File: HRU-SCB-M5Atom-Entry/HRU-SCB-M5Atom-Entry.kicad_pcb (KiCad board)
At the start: 2 copper layers, 25.4 x 50.8 mm, 11 parts, among them J1 GROVE-CONNECTOR-DIP_4P-2.0_

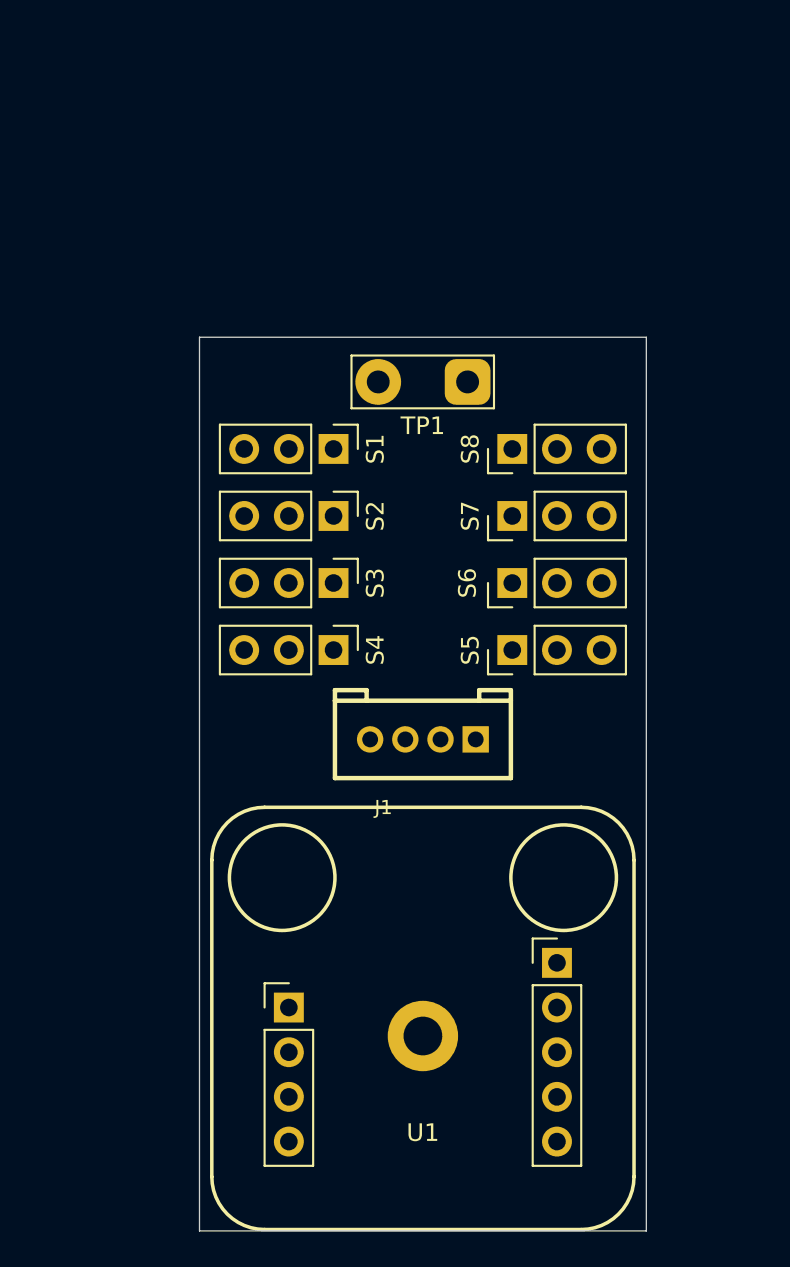
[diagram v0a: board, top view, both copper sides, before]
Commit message: Update: M5Atom entry board with Grove port
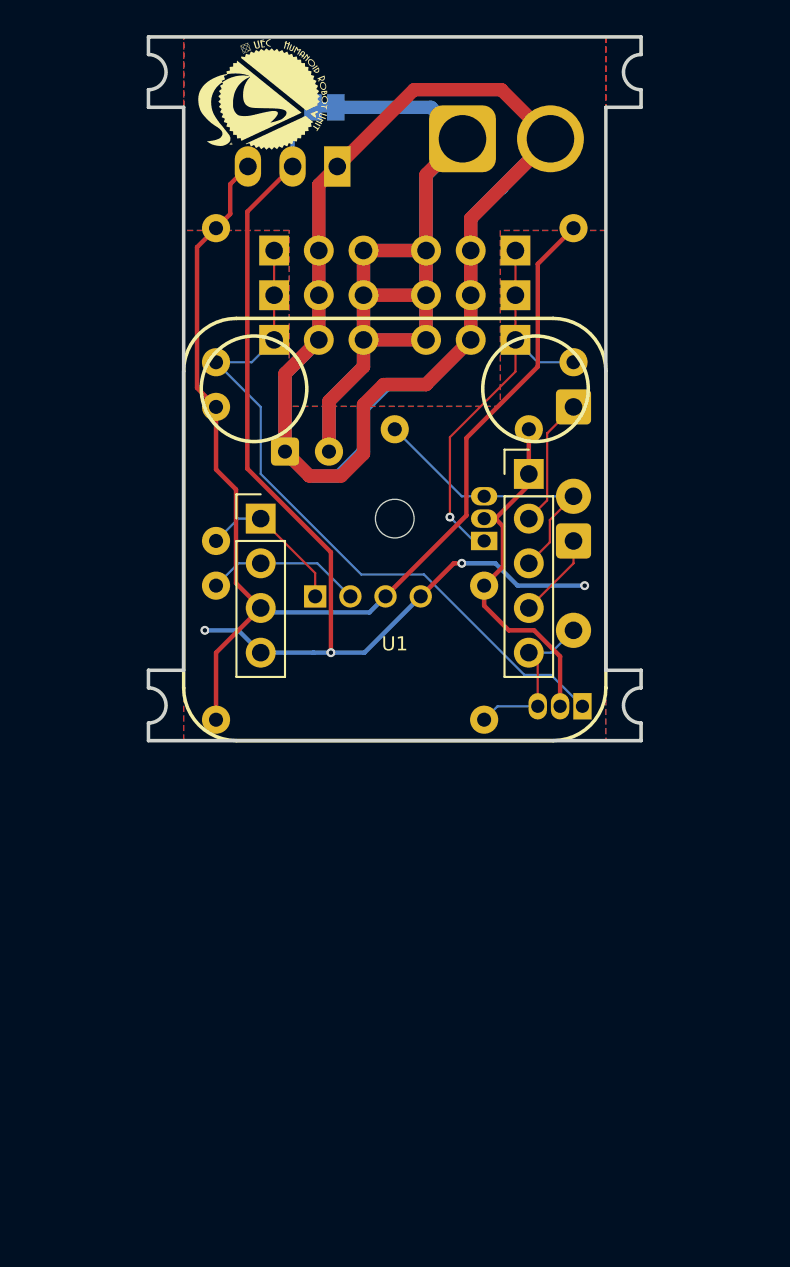
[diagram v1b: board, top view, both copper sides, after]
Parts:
- removed S7, S8: Conn_01x03_Pin, Connector_PinHeader_2.54mm:PinHeader_1x03_P2.54mm_Vertical
- removed TP1: TestPoint_2Pole, TestPoint:TestPoint_2Pads_Pitch5.08mm_Drill1.3mm
- added C1: 220uF, Capacitor_THT:CP_Radial_D6.3mm_P2.50mm, B.Cu at (93.8, 52.2)
- added D1: 11EQS03L, Diode_THT:D_T-1_P5.08mm_Horizontal, B.Cu at (110.2, 49.7)
- added D2: 11EQS03L, Diode_THT:D_T-1_P5.08mm_Horizontal, B.Cu at (110.2, 57.3)
- added J2: GROVE-CONNECTOR-DIP-90D_4P-2.0_, OPL_Connector:GROVE-HW4-2.0-90D, B.Cu at (98.5, 63.6)
- added JP1: SolderJumper_2_Bridged, Jumper:SolderJumper-2_P1.3mm_Bridged_Pad1.0x1.5mm, B.Cu at (96.0, 32.6)
- added Q1: BS170, Package_TO_SOT_THT:TO-92_Inline, B.Cu at (105.1, 57.3)
- added Q2: BS170, Package_TO_SOT_THT:TO-92_Inline, B.Cu at (110.7, 66.7)
- added R1: 2.2k, Resistor_THT:R_Axial_DIN0207_L6.3mm_D2.5mm_P7.62mm_Horizontal, B.Cu at (107.6, 51.0)
- added R2: 2.2k, Resistor_THT:R_Axial_DIN0207_L6.3mm_D2.5mm_P7.62mm_Horizontal, B.Cu at (105.1, 59.8)
- added R3: 2.2k, Resistor_THT:R_Axial_DIN0207_L6.3mm_D2.5mm_P7.62mm_Horizontal, B.Cu at (110.2, 39.5)
- added R4: 2.2k, Resistor_THT:R_Axial_DIN0207_L6.3mm_D2.5mm_P7.62mm_Horizontal, B.Cu at (89.8, 39.5)
- added R5: 2.2k, Resistor_THT:R_Axial_DIN0207_L6.3mm_D2.5mm_P7.62mm_Horizontal, B.Cu at (89.8, 49.7)
- added R6: 2.2k, Resistor_THT:R_Axial_DIN0207_L6.3mm_D2.5mm_P7.62mm_Horizontal, B.Cu at (89.8, 67.5)
- added U2: R-785.0-0.5, Converter_DCDC:Converter_DCDC_RECOM_R-78E-0.5_THT, B.Cu at (96.7, 36.0)
- J1: value GROVE-CONNECTOR-DIP_4P-2.0_ -> Conn_01x02_Pin; footprint OPL_Connector:GROVE-HW4-2.0 -> Connector_AMASS:AMASS_XT30U-M_1x02_P5.0mm_Vertical; moved to B.Cu
- S1, S2, S3, S4, S5, S6: moved to B.Cu
- U1: value ~ -> M5Atom
- moved J1 34.2 mm to (103.8, 34.4), turned to 0 degrees
- moved U1 27.8 mm to (100.0, 63.6)
- moved S5 24.3 mm to (93.1, 43.3), turned to -90 degrees
- moved S6 23.2 mm to (93.1, 40.8), turned to -90 degrees
- moved S4 18.0 mm to (93.1, 45.9)
- moved S3 17.3 mm to (106.9, 45.9), turned to 90 degrees
- moved S2 16.3 mm to (106.9, 43.3), turned to 90 degrees
- moved S1 15.3 mm to (106.9, 40.8), turned to 90 degrees
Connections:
- J1 pad 1: unconnected-(J1-Pad1) -> GNDPWR
- J1 pad 2: unconnected-(J1-Pad2) -> VCC
- S1 pad 1: unconnected-(S1-Pin_1-Pad1) -> /SERVO.0
- S2 pad 1: unconnected-(S2-Pin_1-Pad1) -> /SERVO.0
- S3 pad 1: unconnected-(S3-Pin_1-Pad1) -> /SERVO.0
- S4 pad 1: /SERVO.0 -> /SERVO.1
- S5 pad 1: /SERVO.0 -> /SERVO.1
- S6 pad 1: /SERVO.0 -> /SERVO.1
- U1 pad 1: unconnected-(U1-SCL-Pad1) -> +3V3
- U1 pad 2: unconnected-(U1-SDA-Pad2) -> /Serial.0.TX
- U1 pad 3: unconnected-(U1-5V-Pad3) -> /Serial.0.RX
- U1 pad 4: GND -> /Serial.1.TX
- U1 pad 6: /Serial.1.TX -> GND
- U1 pad 7: /Serial.0.RX -> +5V
- U1 pad 8: /Serial.0.TX -> Net-(U1-SDA)
- U1 pad 9: unconnected-(U1-3V3-Pad9) -> Net-(U1-SCL)
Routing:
- net VCC: track 0.00 -> 108.4 mm
- net GNDPWR: track 0.00 -> 78.9 mm
- net +5V: track 0.00 -> 68.1 mm
- net GND: track 0.00 -> 59.3 mm, vias 0 -> 4
- net /SERVO.1: track 0.00 -> 40.1 mm
- net /SERVO.0: track 0.00 -> 23.0 mm, vias 0 -> 1
- net +3V3: track 0.00 -> 21.1 mm
- net /Serial.0.RX: track 0.00 -> 16.6 mm
- net /Serial.1.RX: track 0.00 -> 9.69 mm
- net Net-(U1-SDA): track 0.00 -> 8.94 mm
- net Net-(U1-SCL): track 0.00 -> 8.77 mm
- net /Serial.0.TX: track 0.00 -> 7.40 mm
- net /Serial.1.TX: track 0.00 -> 4.86 mm
- added copper zone on B.Cu, net GND
- added copper zone on F.Cu, net GND
- added copper zone on B.Cu, net GNDPWR
- added copper zone on F.Cu, net VCC
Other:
- board size 25.4 x 50.8 mm -> 28 x 40 mm
- board text added: "CH0"
- board text added: "CH1"
- board text added: "G"
- board text added: "V"

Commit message: Update: parts layout and smaller board
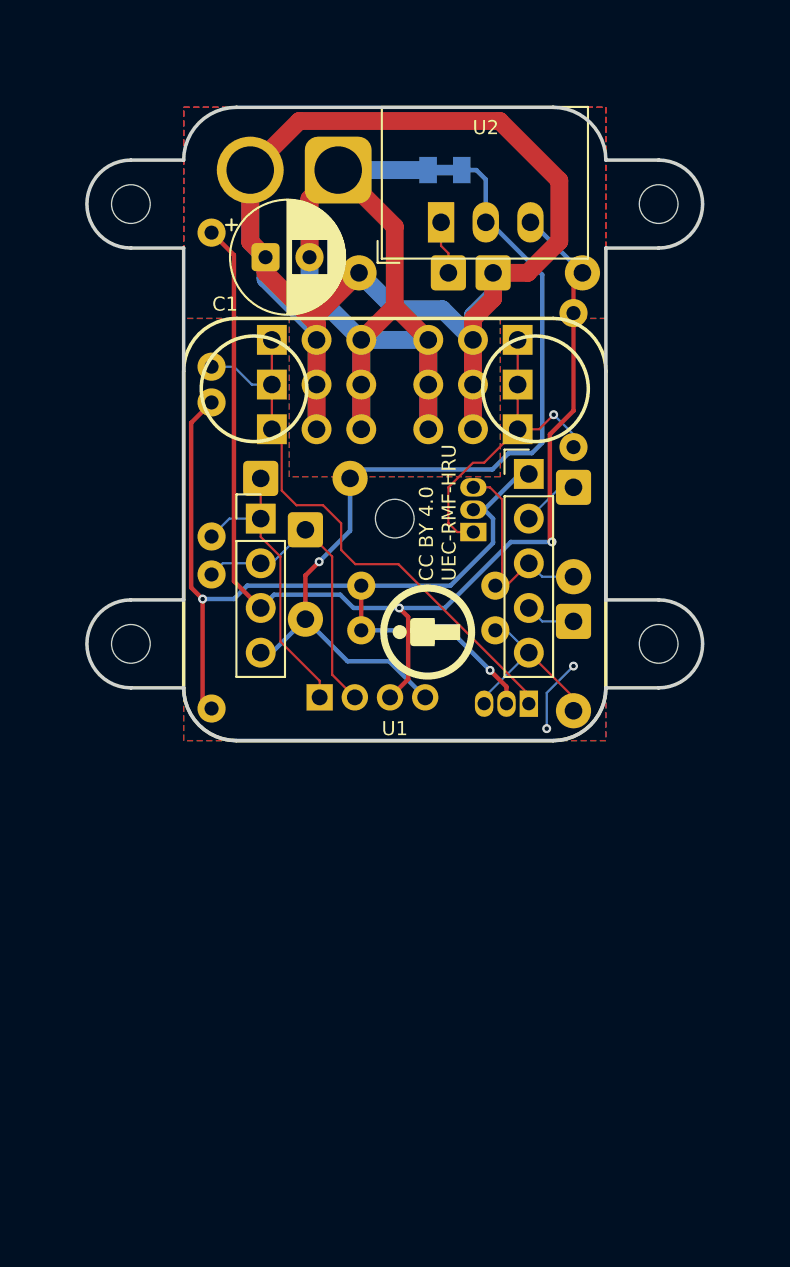
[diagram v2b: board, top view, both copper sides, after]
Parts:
- added D3: BZX55C3V3, Diode_THT:D_T-1_P5.08mm_Horizontal, B.Cu at (92.4, 53.7)
- added D4: BZX55C3V3, Diode_THT:D_T-1_P5.08mm_Horizontal, B.Cu at (94.9, 56.7)
- added D5: 11EQS03L, Diode_THT:D_T-1_P5.08mm_Horizontal, B.Cu at (103.0, 42.1)
- added D6: 11EQS03L, Diode_THT:D_T-1_P5.08mm_Horizontal, B.Cu at (105.6, 42.1)
- added H1: MountingHole, MountingHole:MountingHole_2.2mm_M2, F.Cu at (85.0, 38.1)
- added H2: MountingHole, MountingHole:MountingHole_2.2mm_M2, F.Cu at (115.0, 38.1)
- added H3: MountingHole, MountingHole:MountingHole_2.2mm_M2, F.Cu at (115.0, 63.1)
- added H4: MountingHole, MountingHole:MountingHole_2.2mm_M2, F.Cu at (85.0, 63.1)
- added REF**: Symbol_CC-Attribution_CopperTop_Small, Symbol:Symbol_CC-Attribution_CopperTop_Small, F.Cu at (101.9, 62.5)
- C1, U2: moved to F.Cu
- J2: value GROVE-CONNECTOR-DIP-90D_4P-2.0_ -> GROVE-CONNECTOR-DIP_4P-2.0_; footprint OPL_Connector:GROVE-HW4-2.0-90D -> OPL_Connector:GROVE-HW4-2.0
- moved R1 13.0 mm to (98.1, 59.8), turned to 0 degrees
- moved C1 11.1 mm to (92.7, 41.2)
- moved JP1 7.45 mm to (102.5, 36.2), turned to 0 degrees
- moved R2 7.43 mm to (98.1, 62.4), turned to 0 degrees
- moved J1 7.29 mm to (96.8, 36.2), turned to 180 degrees
- moved U2 6.70 mm to (102.6, 39.2), turned to 0 degrees
- moved S3 5.08 mm to (107.0, 51.0)
- moved S4 5.08 mm to (93.0, 51.0)
- moved S1 5.08 mm to (107.0, 45.9)
- moved S2 5.08 mm to (107.0, 48.4)
- moved S5 5.08 mm to (93.0, 48.4)
- moved S6 5.08 mm to (93.0, 45.9)
- moved R3 4.83 mm to (110.2, 44.3)
- moved D1 4.57 mm to (110.2, 54.3)
- moved D2 4.57 mm to (110.2, 61.9)
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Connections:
- R5 pad 1: +5V -> +3V3
- R6 pad 1: +5V -> +3V3
- U2 pad 1: VCC -> Net-(D5-K)
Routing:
- net +3V3: track 21.1 -> 56.0 mm, vias 0 -> 2
- net GNDPWR: track 78.9 -> 61.2 mm
- net VCC: track 108.4 -> 92.3 mm
- net Net-(D3-K): track 8.77 -> 17.0 mm
- net Net-(D4-K): track 8.94 -> 17.1 mm
- net /SERVO.1: track 40.1 -> 32.9 mm
- net /Serial.0.RX: track 16.6 -> 12.3 mm
- net GND: track 59.3 -> 55.0 mm, vias 4 -> 3
- net /Serial.0.TX: track 7.40 -> 3.28 mm
- net /SERVO.0: track 23.0 -> 19.5 mm
- net Net-(D5-K): track 0.00 -> 3.04 mm
- net /Serial.1.TX: track 4.86 -> 2.86 mm
- net /Serial.1.RX: track 9.69 -> 10.7 mm
- net +5V: track 68.1 -> 67.2 mm, vias 0 -> 2
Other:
- board size 28 x 40 mm -> 35 x 36 mm
- board text added: "CC BY 4.0 UEC-RMF-HRU"
- board text added: "HRU-SCB-M5Atom-Entry"

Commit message: update: non-via circuit
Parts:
- removed REF**: Symbol_CC-Attribution_CopperTop_Small, Symbol:Symbol_CC-Attribution_CopperTop_Small
- S1, S2, S3, S4, S5, S6: footprint Connector_PinHeader_2.54mm:PinHeader_1x03_P2.54mm_Vertical -> mymod:PinHeader_1x03_P2.54mm_Vertical_SmallCourtyard
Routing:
- net +5V: track 67.2 -> 74.3 mm, vias 2 -> 0
- net +3V3: track 56.0 -> 52.7 mm, vias 2 -> 0
- net /SERVO.0: track 19.5 -> 17.0 mm, vias 1 -> 0
- net Net-(D3-K): track 17.0 -> 19.4 mm
- net /Serial.0.RX: track 12.3 -> 11.3 mm
- net GND: track 55.0 -> 56.0 mm, vias 3 -> 0
- net /SERVO.1: track 32.9 -> 33.5 mm

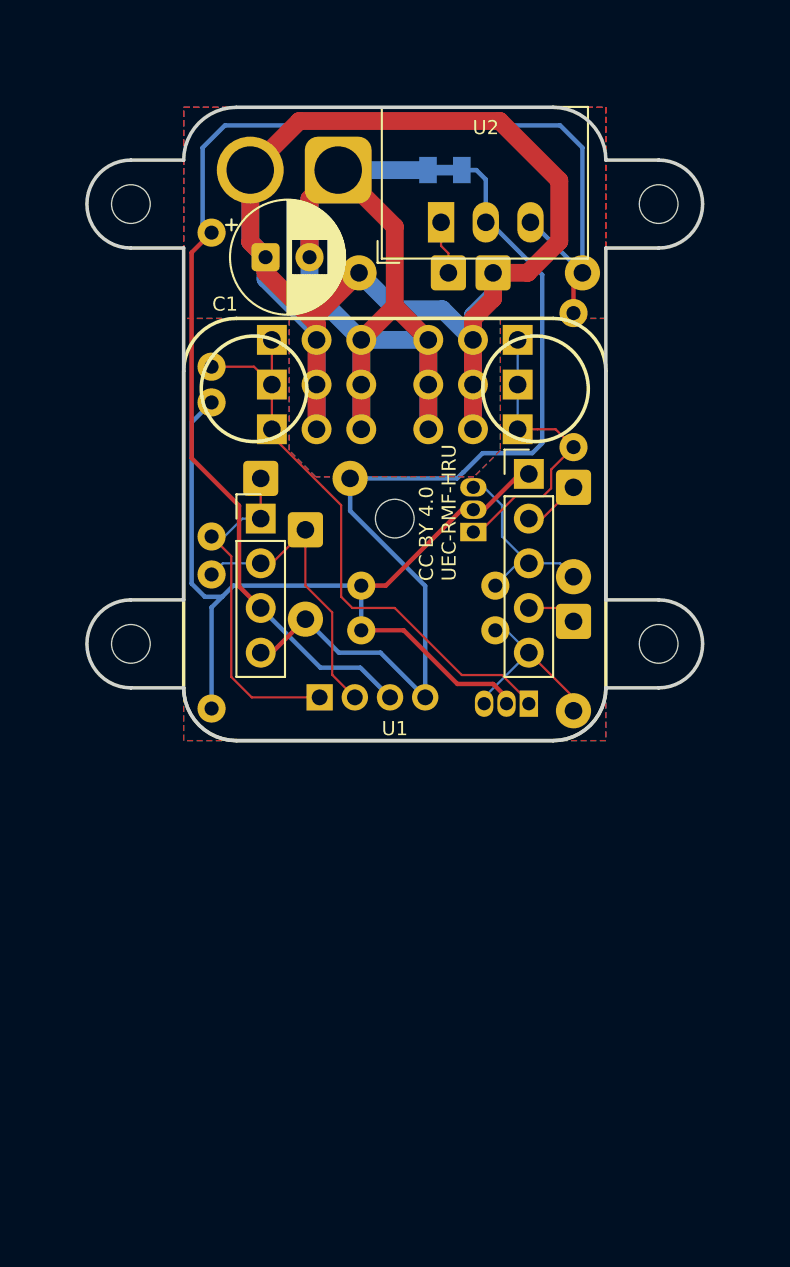
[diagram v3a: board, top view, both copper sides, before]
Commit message: update: larger board outline for flesh members
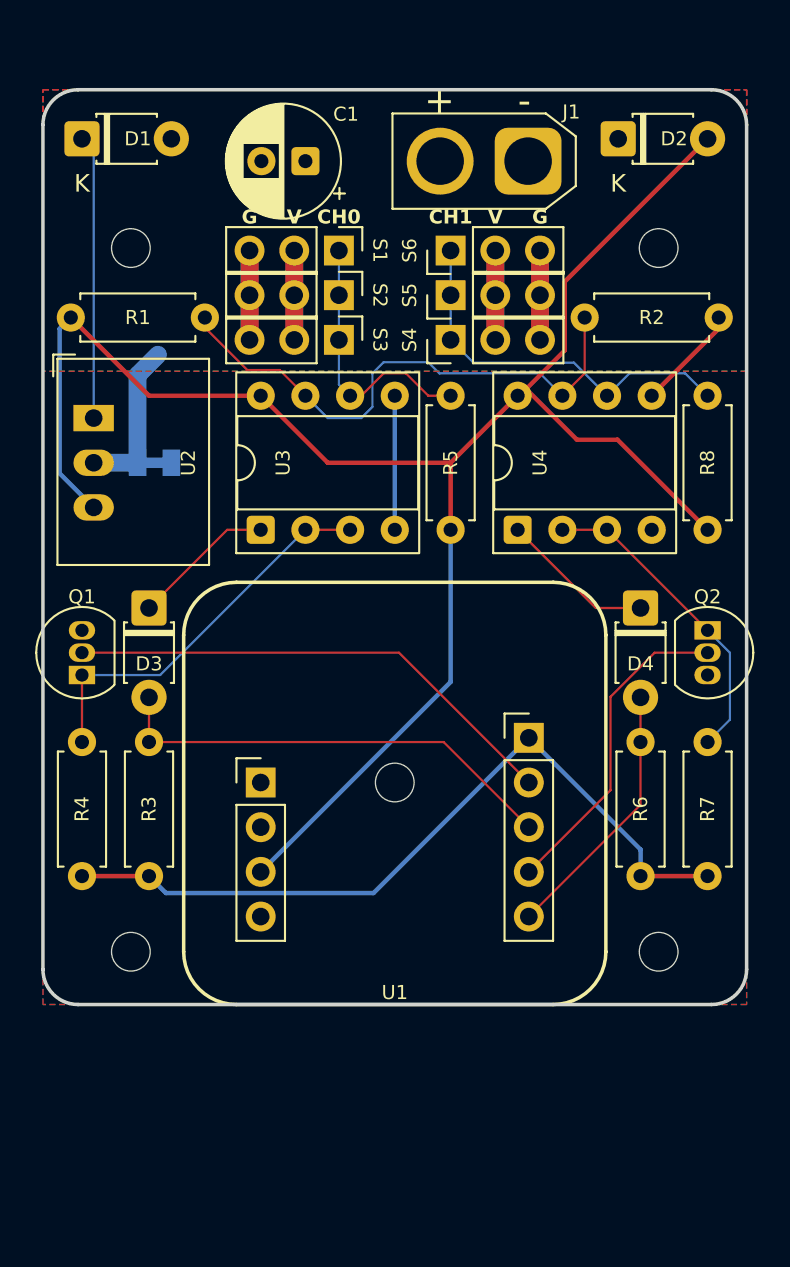
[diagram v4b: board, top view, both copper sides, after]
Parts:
- removed D5, D6: 11EQS03L, Diode_THT:D_T-1_P5.08mm_Horizontal
- removed J2: GROVE-CONNECTOR-DIP_4P-2.0_, OPL_Connector:GROVE-HW4-2.0
- added R7: 2.2k, Resistor_THT:R_Axial_DIN0207_L6.3mm_D2.5mm_P7.62mm_Horizontal, F.Cu at (117.8, 76.3)
- added R8: 2.2k, Resistor_THT:R_Axial_DIN0207_L6.3mm_D2.5mm_P7.62mm_Horizontal, F.Cu at (117.8, 56.7)
- added U3: MAX485E, Package_DIP:DIP-8_W7.62mm_Socket, F.Cu at (92.4, 56.7)
- added U4: MAX485E, Package_DIP:DIP-8_W7.62mm_Socket, F.Cu at (107.0, 56.7)
- D1, D2, J1, Q1, Q2, R1, R2, R3, R4, R5, R6, S1, S2, S3, S4, S5, S6: moved to F.Cu
- D3, D4: value BZX55C3V3 -> 11EQS03L; moved to F.Cu
- moved R3 40.1 mm to (86.0, 76.3), turned to 90 degrees
- moved R4 37.3 mm to (82.2, 76.3), turned to 90 degrees
- moved D1 34.3 mm to (82.2, 34.4), turned to 0 degrees
- moved D2 27.5 mm to (112.7, 34.4), turned to 0 degrees
- moved R6 26.2 mm to (114.0, 76.3)
- moved Q1 23.7 mm to (82.2, 64.9)
- moved JP1 23.4 mm to (86.0, 52.9)
- moved U2 22.7 mm to (82.9, 50.3), turned to -90 degrees
- moved R1 22.5 mm to (81.6, 44.6)
- moved R2 21.8 mm to (110.8, 44.6)
- moved D4 19.6 mm to (114.0, 61.1)
- moved H3 17.5 mm to (115.0, 80.7)
- moved H4 17.5 mm to (85.0, 80.7)
- moved R5 15.4 mm to (103.2, 56.7), turned to 90 degrees
- moved U1 15.0 mm to (100.0, 78.7)
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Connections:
- D1 pad 1: /Serial.0.TX -> Net-(D1-K)
- D1 pad 2: /Serial.0.RX -> VCC
- D2 pad 1: /Serial.1.TX -> VCC
- D2 pad 2: /Serial.1.RX -> +5V
- D3 pad 2: GND -> /Serial.0.RX
- D4 pad 2: GND -> /Serial.1.RX
- Q1 pad 1: /SERVO.0 -> Net-(Q1-D)
- Q1 pad 2: +3V3 -> /Serial.0.TX
- Q1 pad 3: /Serial.0.RX -> GND
- Q2 pad 1: /SERVO.1 -> Net-(Q2-D)
- Q2 pad 2: +3V3 -> /Serial.1.TX
- Q2 pad 3: /Serial.1.RX -> GND
- R1 pad 1: +3V3 -> +5V
- R1 pad 2: /Serial.0.RX -> /2V5
- R2 pad 1: +3V3 -> /2V5
- R2 pad 2: /Serial.1.RX -> GND
- R3 pad 1: +5V -> +3V3
- R3 pad 2: /SERVO.0 -> /Serial.0.RX
- R4 pad 1: +5V -> +3V3
- R4 pad 2: /SERVO.1 -> Net-(Q1-D)
- R5 pad 1: +3V3 -> +5V
- R5 pad 2: Net-(D3-K) -> /SERVO.0
- R6 pad 2: Net-(D4-K) -> /Serial.1.RX
- U1 pad 8: Net-(D4-K) -> unconnected-(U1-SDA-Pad8)
- U1 pad 9: Net-(D3-K) -> unconnected-(U1-SCL-Pad9)
- U2 pad 1: Net-(D5-K) -> Net-(D1-K)
- U2 pad 2: GND -> GNDPWR
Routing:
- net VCC: track 92.3 -> 20.3 mm
- net GND: track 56.0 -> 13.6 mm
- net GNDPWR: track 61.2 -> 29.4 mm
- net /2V5: track 0.00 -> 31.2 mm
- net +5V: track 74.3 -> 102.7 mm
- net /Serial.0.TX: track 3.28 -> 28.5 mm
- net Net-(Q1-D): track 0.00 -> 22.5 mm
- net Net-(Q2-D): track 0.00 -> 18.0 mm
- net Net-(D1-K): track 0.00 -> 16.2 mm
- net /Serial.1.TX: track 2.86 -> 18.4 mm
- net /Serial.0.RX: track 11.3 -> 26.1 mm
- net /SERVO.1: track 33.5 -> 22.1 mm
- net Net-(D3-K): track 19.4 -> 8.19 mm
- net +3V3: track 52.7 -> 43.8 mm
- net Net-(D4-K): track 17.1 -> 8.83 mm
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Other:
- board size 35 x 36 mm -> 40 x 52 mm

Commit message: Update: PCB wires
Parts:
- moved C1 0.78 mm to (94.3, 35.2)
- moved J1 0.25 mm to (107.6, 35.5)
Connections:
- U1 pad 2: /Serial.0.TX -> /Serial.0.RX
- U1 pad 3: /Serial.0.RX -> /Serial.0.TX
- U1 pad 4: /Serial.1.TX -> /Serial.1.RX
- U1 pad 5: /Serial.1.RX -> /Serial.1.TX
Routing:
- net GND: track 13.6 -> 6.02 mm
- net /Serial.0.TX: track 28.5 -> 35.6 mm
- net +5V: track 102.7 -> 105.3 mm
- net /Serial.1.RX: track 15.1 -> 12.6 mm
- net /Serial.1.TX: track 18.4 -> 19.8 mm
- net /2V5: track 31.2 -> 30.0 mm
- net /Serial.0.RX: track 26.1 -> 25.1 mm
- net +3V3: track 43.8 -> 43.0 mm
